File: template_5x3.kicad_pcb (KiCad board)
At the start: 2 copper layers, 120.7 x 66 mm, 1 part

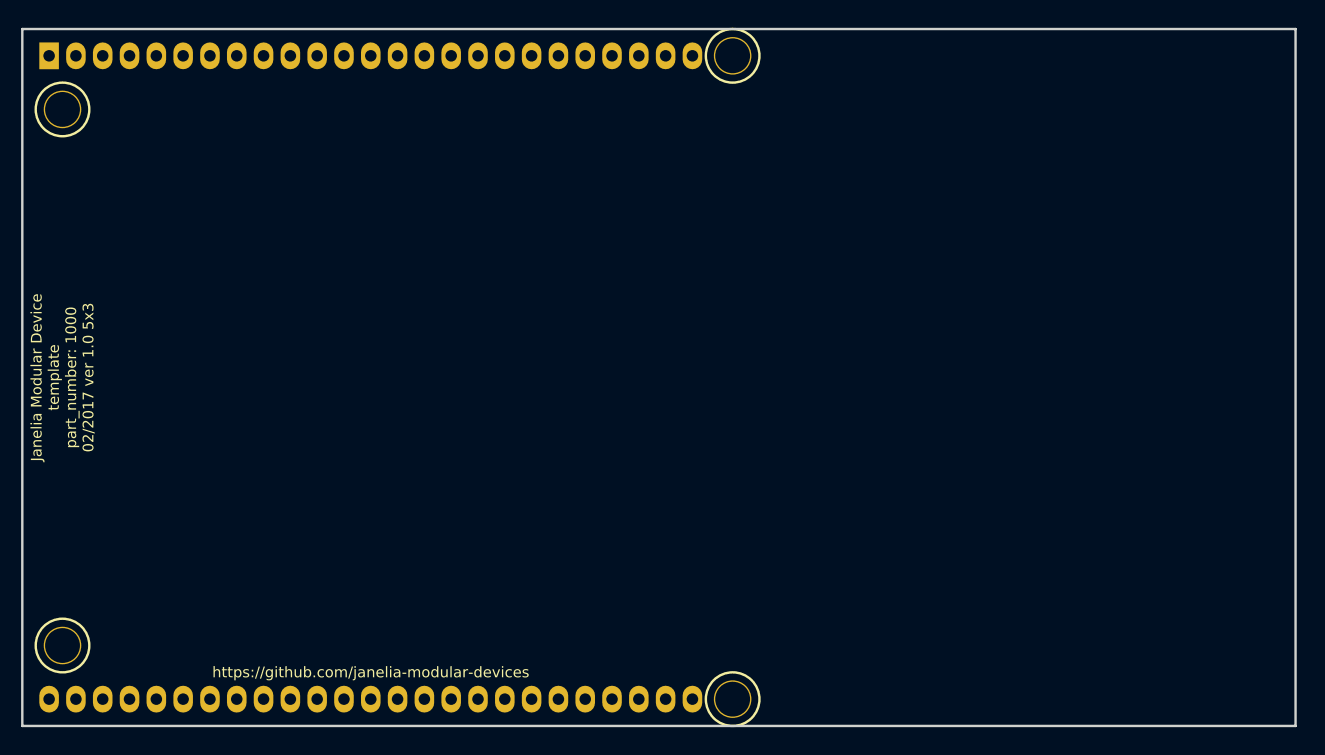
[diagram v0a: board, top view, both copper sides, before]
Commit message: Updated template files.
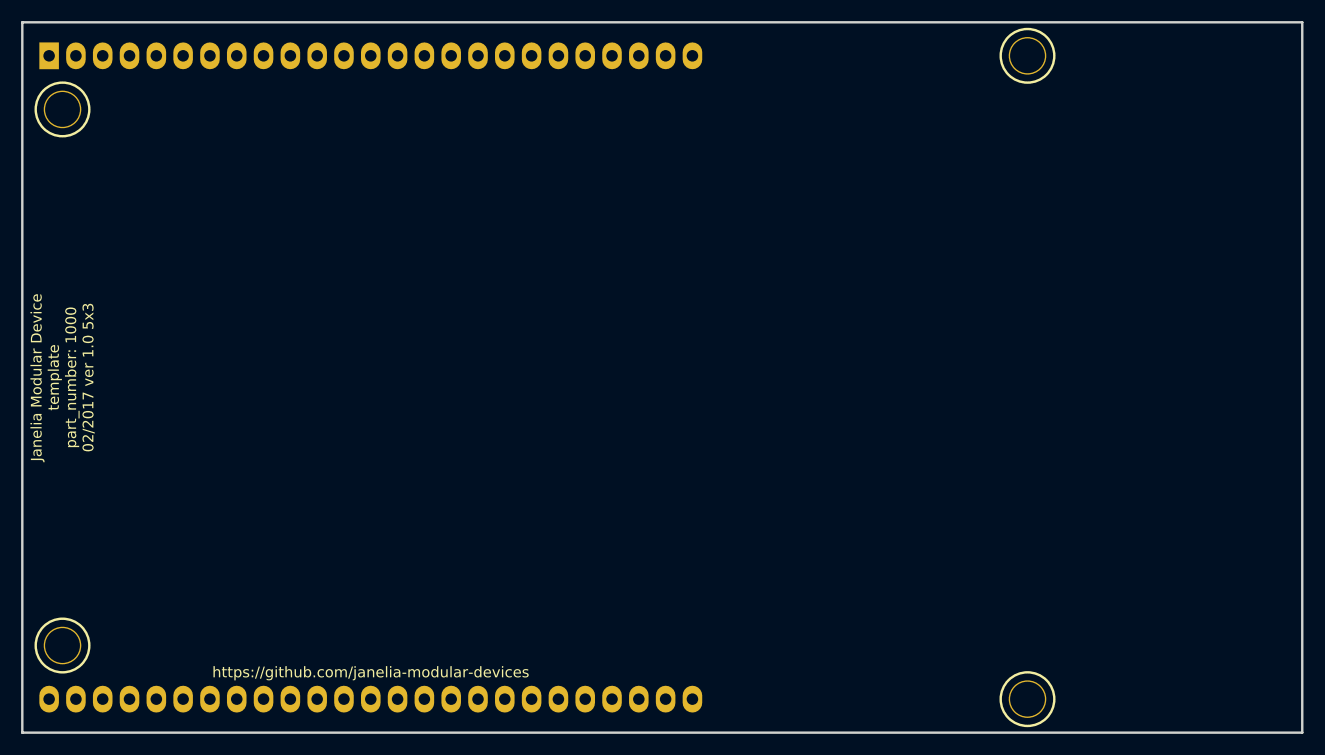
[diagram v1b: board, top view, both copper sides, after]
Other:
- board size 120.7 x 66 mm -> 121.3 x 67.3 mm
